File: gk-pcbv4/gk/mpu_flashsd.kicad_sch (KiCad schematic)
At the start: 26 parts, among them J3 Bus_M.2_Socket_E, J4 Micro_SD_Card_Det2, U5 STM32MP255DAI3, U7 W25Q32JVSN

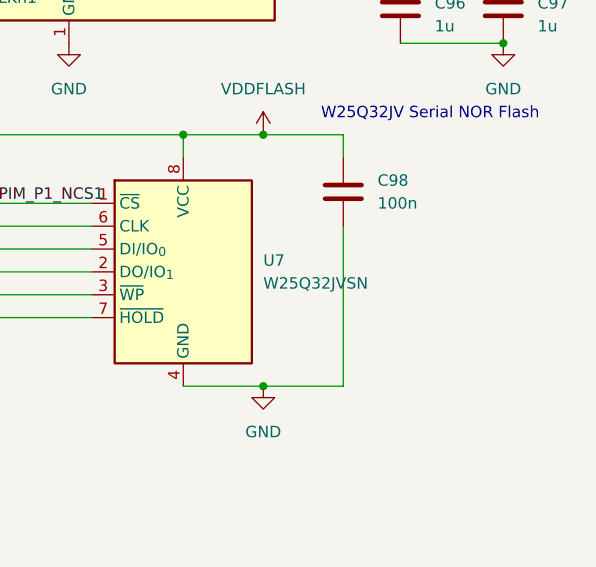
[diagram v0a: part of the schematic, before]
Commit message: add option for larger qspi flash
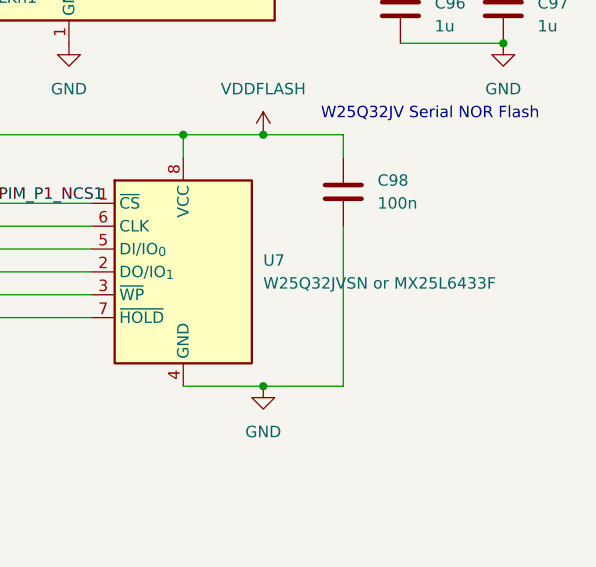
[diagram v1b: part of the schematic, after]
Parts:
- U7: value W25Q32JVSN -> W25Q32JVSN or MX25L6433F
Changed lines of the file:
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@@
 			)
 		)
-		(property "Value" "W25Q32JVSN"
+		(property "Value" "W25Q32JVSN or MX25L6433F"
 			(at 248.92 148.5899 0)
 			(effects

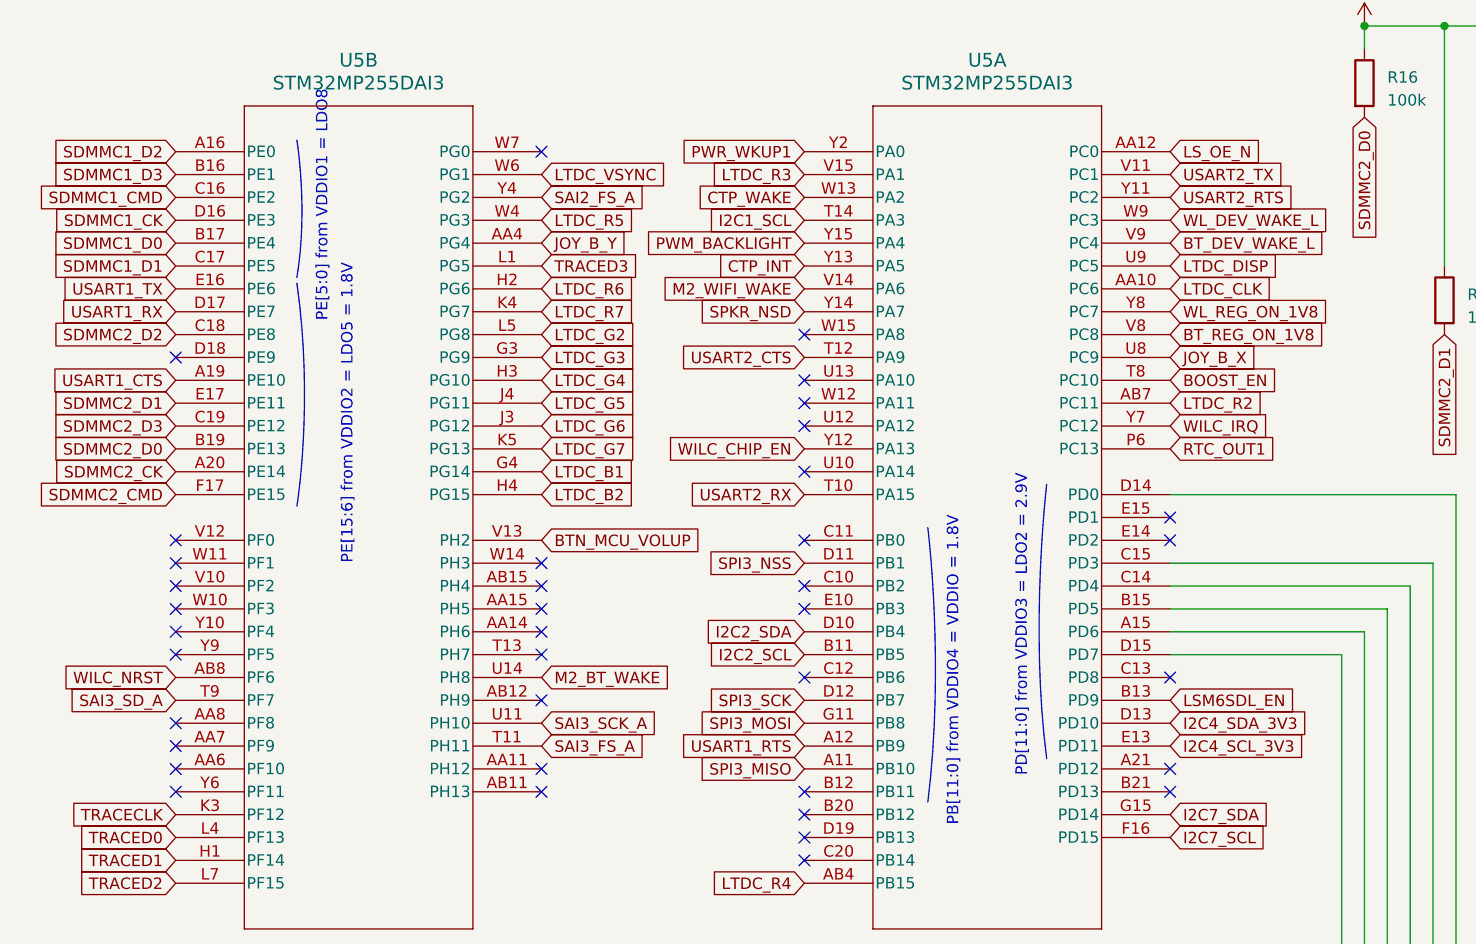
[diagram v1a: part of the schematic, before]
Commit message: add usart6 connection to schematic
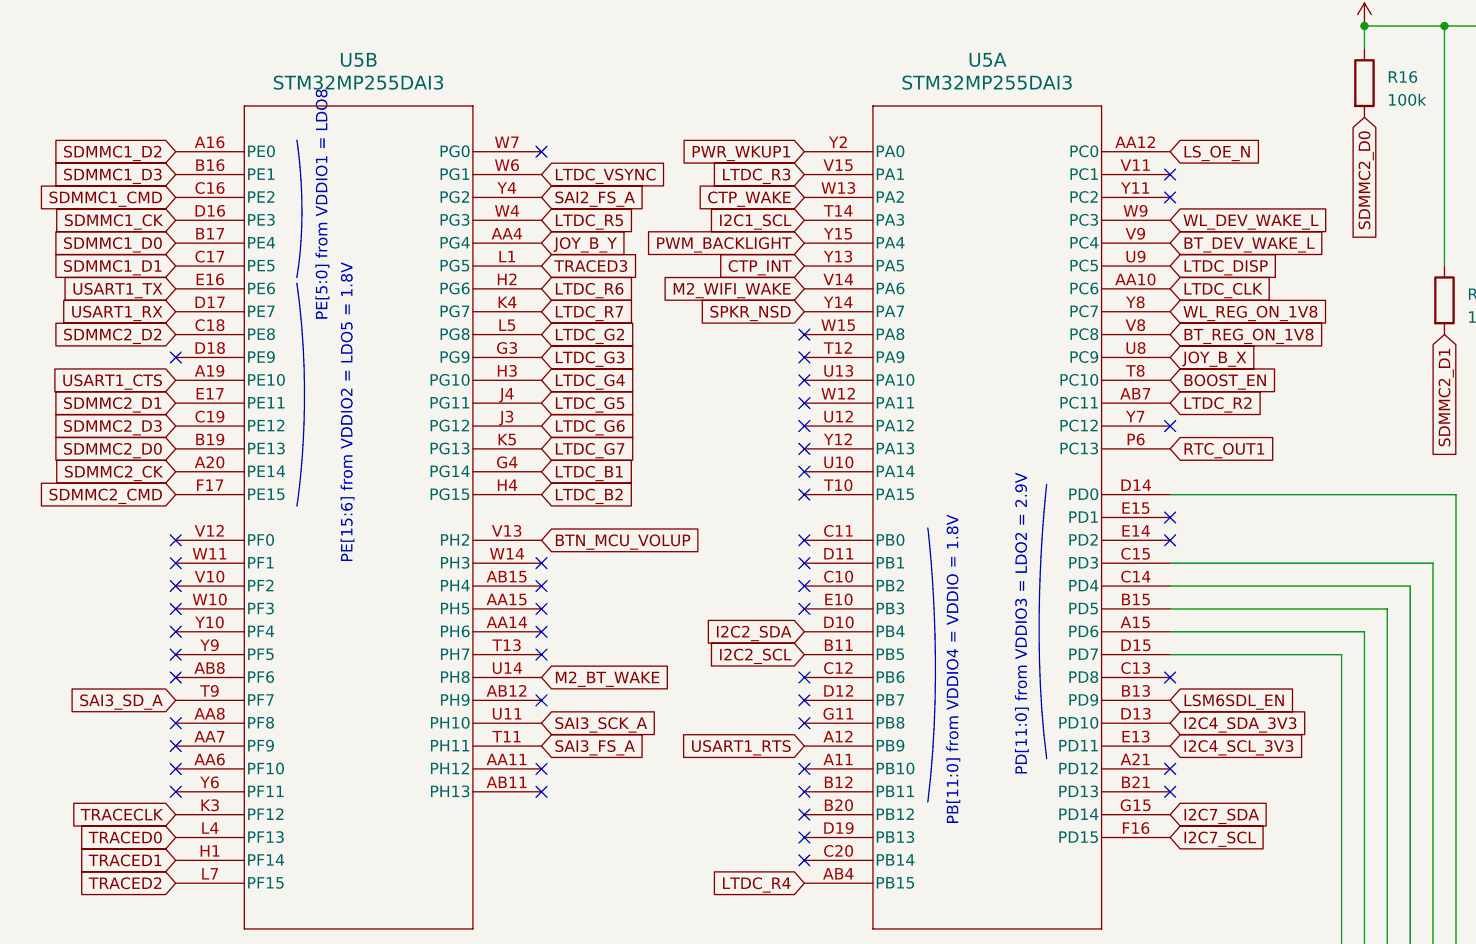
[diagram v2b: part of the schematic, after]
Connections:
- net SPI3_MISO: no longer names the net of U5.A11 (PB10)
- net SPI3_MOSI: no longer names the net of U5.G11 (PB8)
- net SPI3_NSS: no longer names the net of U5.D11 (PB1)
- net SPI3_SCK: no longer names the net of U5.D12 (PB7)
- net USART2_CTS: no longer names the net of U5.T12 (PA9)
- net USART2_RTS: no longer names the net of U5.Y11 (PC2)
- net USART2_RX: no longer names the net of U5.T10 (PA15)
- net USART2_TX: no longer names the net of U5.V11 (PC1)
- net WILC_CHIP_EN: no longer names the net of U5.Y12 (PA13)
- net WILC_IRQ: no longer names the net of U5.Y7 (PC12)
- net WILC_NRST: no longer names the net of U5.AB8 (PF6)
- no-connect marks 72 -> 83

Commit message: Add throttle control
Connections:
- net JOY_THROTTLE: now reaches U5.V12 (PF0)
- no-connect marks 83 -> 82
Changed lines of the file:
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@@
-	)
-	(no_connect
-		(at 34.29 80.01)
 	)
 	(no_connect
@@
 				(hide yes)
 			)
+		)
+	)
+	(global_label "JOY_THROTTLE"
+		(shape input)
+		(at 34.29 80.01 180)
+		(fields_autoplaced yes)
+		(effects
+			(font
+				(size 1.27 1.27)
+			)
+			(justify right)
+		)
+		(property "Intersheetrefs" "${INTERSHEET_REFS}"
+			(at 17.9396 80.01 0)
+			(effects
+				(font
+					(size 1.27 1.27)
+				)
+				(justify right)
+				(hide yes)
+			)

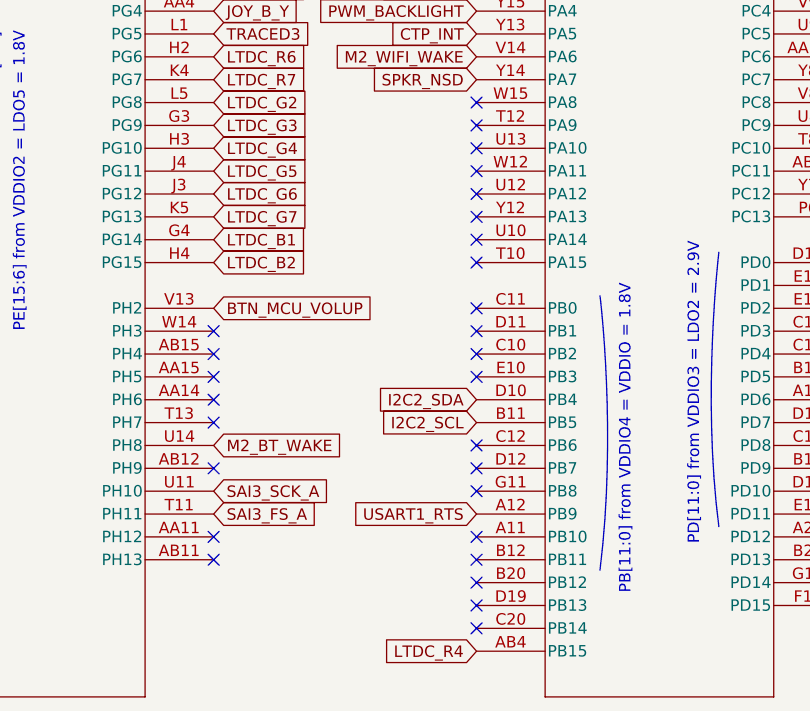
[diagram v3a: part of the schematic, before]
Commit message: move LB/RB to main board
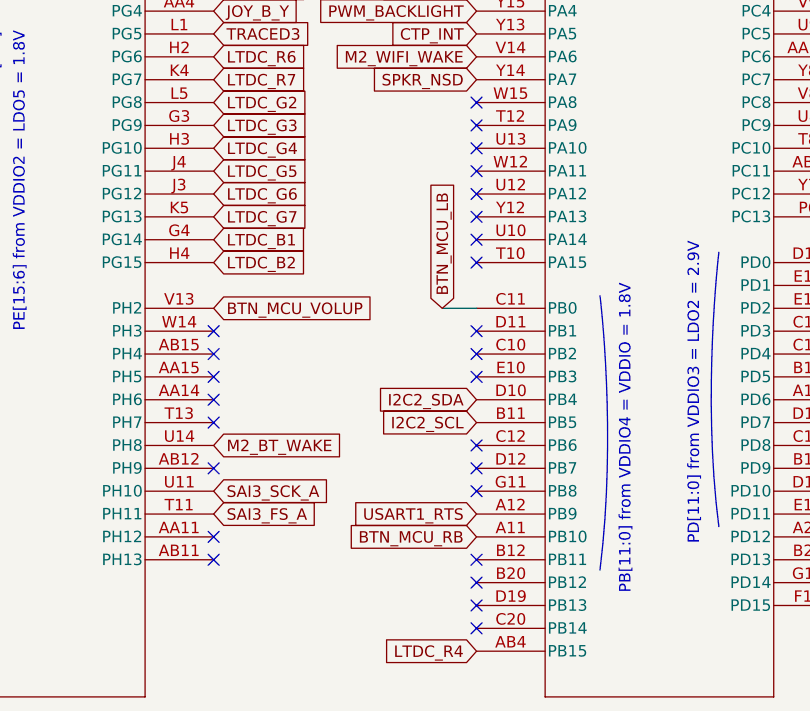
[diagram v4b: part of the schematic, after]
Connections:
- net BTN_MCU_RB: now reaches U5.A11 (PB10)
- net BTN_MCU_LB: now reaches U5.C11 (PB0)
- no-connect marks 82 -> 80
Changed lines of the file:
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@@
 	)
 	(no_connect
-		(at 104.14 80.01)
-	)
-	(no_connect
 		(at 144.78 67.31)
 	)
@@
 	)
 	(no_connect
-		(at 104.14 105.41)
-	)
-	(no_connect
 		(at 252.73 50.8)
 	)
@@
 	(wire
 		(pts
+			(xy 100.33 80.01) (xy 104.14 80.01)
+		)
+		(stroke
+			(width 0)
+			(type default)
+		)
+	)
+	(wire
+		(pts
 			(xy 190.5 22.86) (xy 194.31 22.86)
 		)
@@
 		)
 	)
+	(global_label "BTN_MCU_RB"
+		(shape input)
+		(at 104.14 105.41 180)
+		(fields_autoplaced yes)
+		(effects
+			(font
+				(size 1.27 1.27)
+			)
+			(justify right)
+		)
+		(property "Intersheetrefs" "${INTERSHEET_REFS}"
+			(at 89.0596 105.41 0)
+			(effects
+				(font
+					(size 1.27 1.27)
+				)
+				(justify right)
+				(hide yes)
+			)
+		)
+	)
 	(global_label "USART1_TX"
 		(shape input)
@@
 				(hide yes)
 			)
+		)
+	)
+	(global_label "BTN_MCU_LB"
+		(shape input)
+		(at 100.33 80.01 90)
+		(fields_autoplaced yes)
+		(effects
+			(font
+				(size 1.27 1.27)
+			)
+			(justify left)
+		)
+		(property "Intersheetrefs" "${INTERSHEET_REFS}"
+			(at 100.33 65.1715 90)
+			(effects
+				(font
+					(size 1.27 1.27)
+				)
+				(justify left)
+				(hide yes)
+			)
